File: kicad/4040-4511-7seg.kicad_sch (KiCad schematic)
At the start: 3 parts, among them U10 4511, U11 D168K, U12 4040

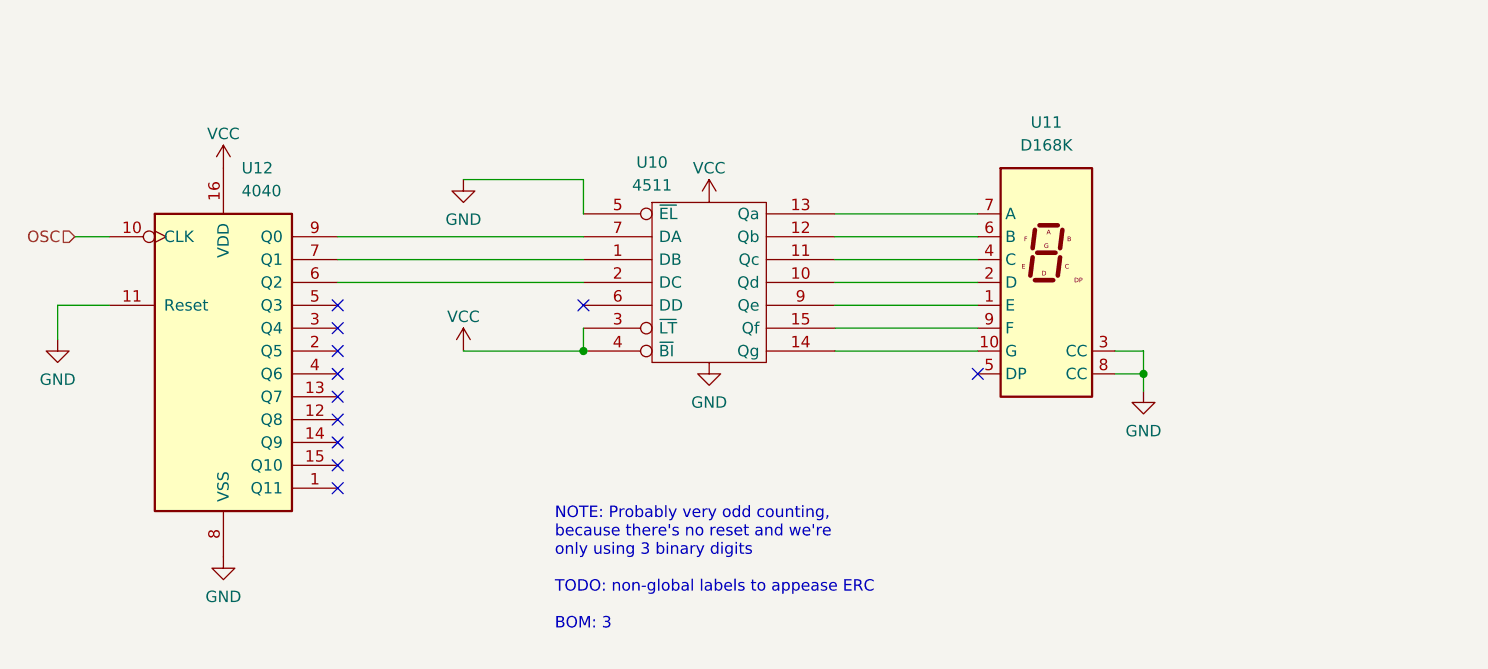
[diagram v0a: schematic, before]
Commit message: Hmmm, may need resistors for LED driver ICs
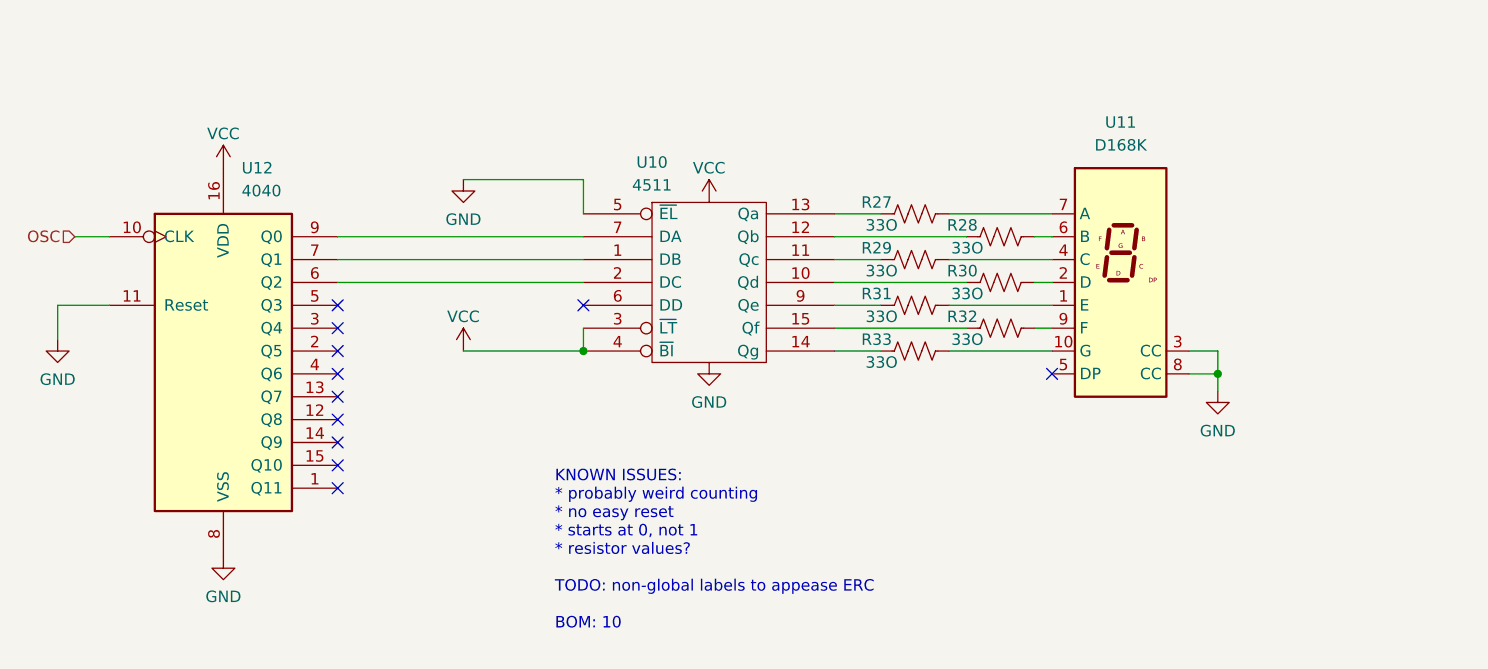
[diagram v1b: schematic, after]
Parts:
- added R27, R28, R29, R30, R31, R32, R33: 33O, Resistor_THT:R_Axial_DIN0204_L3.6mm_D1.6mm_P7.62mm_Horizontal, symbol Device:R_US
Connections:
- net at U10.10 (Qd): now also R30.1; no longer U11.2 (D)
- net at U10.11 (Qc): now also R29.1; no longer U11.4 (C)
- net at U10.12 (Qb): now also R28.1; no longer U11.6 (B)
- net at U10.13 (Qa): now also R27.1; no longer U11.7 (A)
- net at U10.14 (Qg): now also R33.1; no longer U11.10 (G)
- net at U10.15 (Qf): now also R32.1; no longer U11.9 (F)
- net at U10.9 (Qe): now also R31.1; no longer U11.1 (E)
- new net: R28.2, U11.6 (B)
- new net: R33.2, U11.10 (G)
- new net: R30.2, U11.2 (D)
- new net: R32.2, U11.9 (F)
- new net: R31.2, U11.1 (E)
- new net: R29.2, U11.4 (C)
- new net: R27.2, U11.7 (A)
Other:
- note added: "KNOWN ISSUES: * probably weird counting * no easy reset * starts at 0, not 1 * resistor values? TODO: non-global labels to appease ERC BOM: 10"
- note removed: "NOTE: Probably very odd counting, because there's no reset and we're only using 3 binary digits TODO: non-global labels to appease ERC BOM: 3"

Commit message: TODO: fix 7seg footprint
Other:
- note added: "TODO: fix footprint! 10 A 9 B 7 C 5 D 4 E 2 F 1 G 6 DP 3 COM 8 COM"
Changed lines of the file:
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@@
+    (effects (font (size 1.27 1.27)) (justify left bottom))
+  )
+  (text "TODO: fix footprint!\n\n10 A\n9  B\n7  C\n5  D\n4  E\n2  F\n1  G\n\n6  DP\n3  COM\n8  COM"
+    (at 215.265 83.82 0)
     (effects (font (size 1.27 1.27)) (justify left bottom))
   )

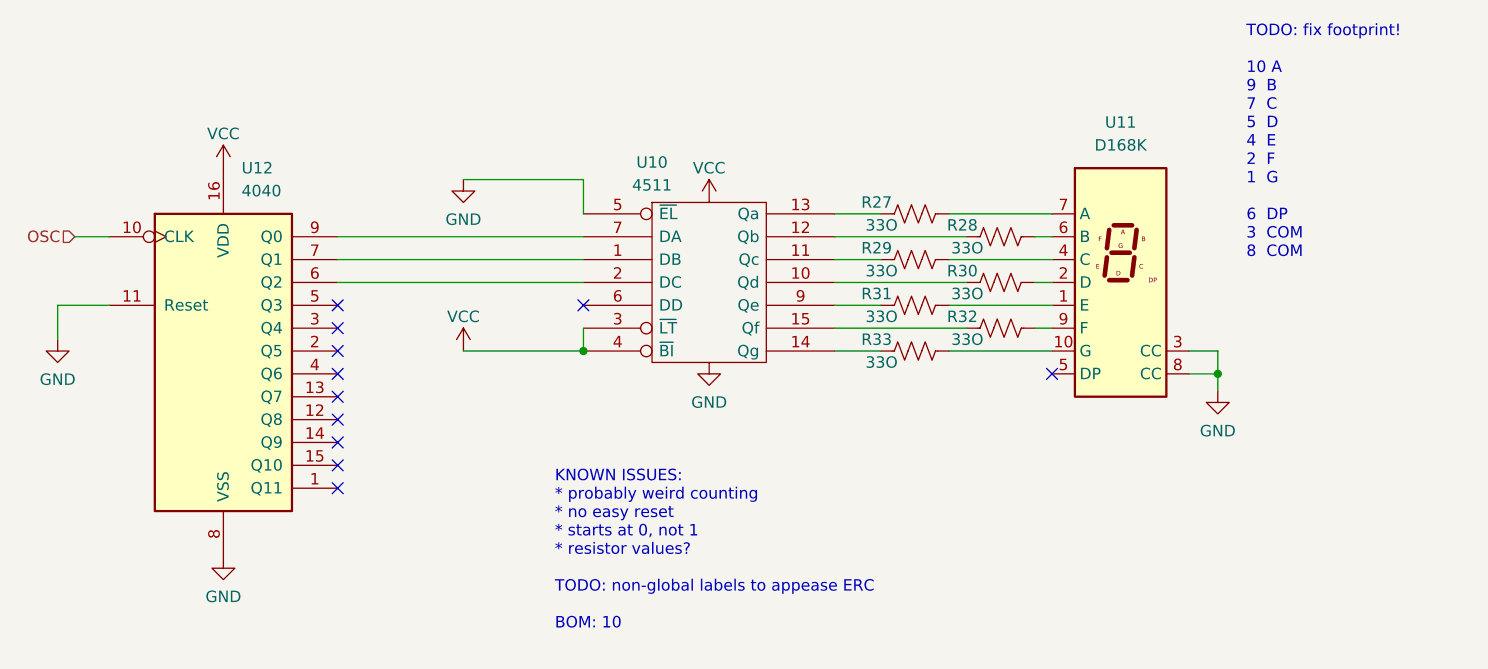
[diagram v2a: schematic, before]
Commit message: Fix 7seg footprint
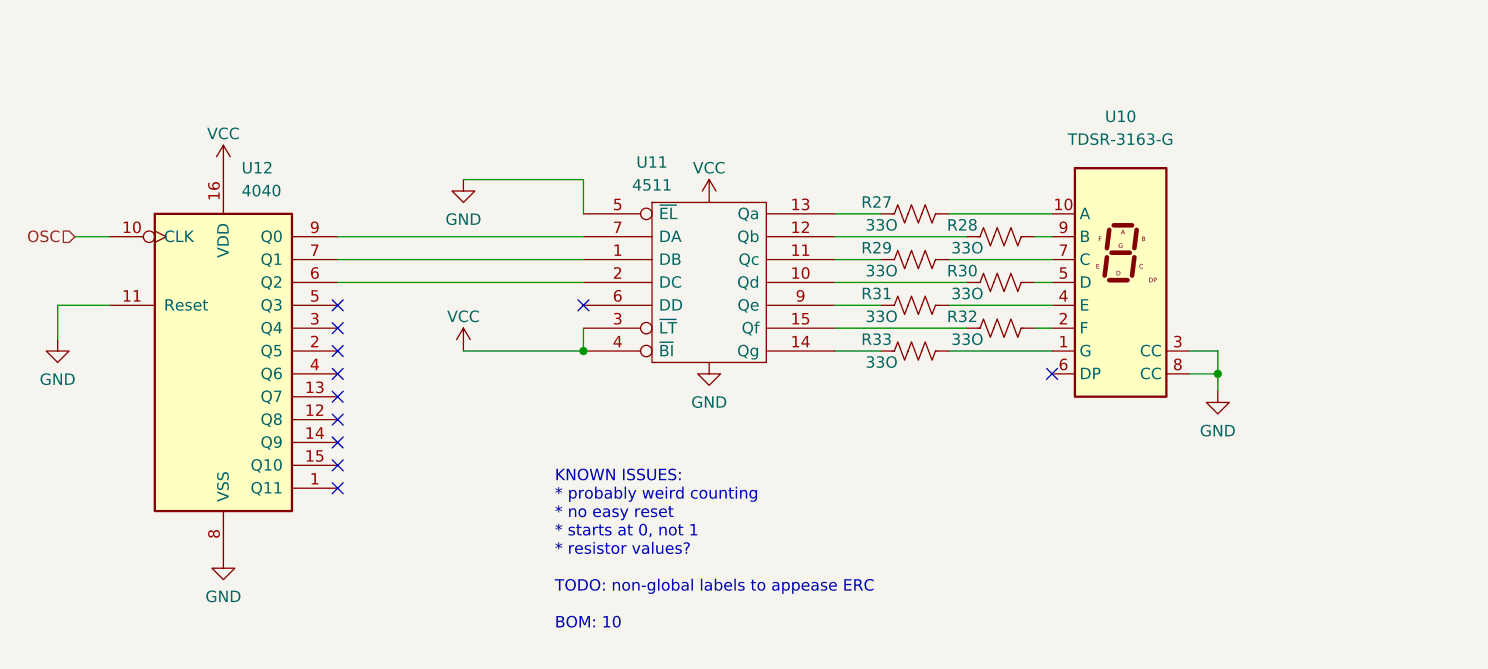
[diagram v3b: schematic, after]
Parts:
- removed U11: D168K, Display_7Segment:D1X8K, symbol Display_Character:D168K
- added U10: TDSR-3163-G, symbol parts_cafe:TDSR-3163-G
- renumbered U10 to U11
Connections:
- net GND: now also U10.3 (CC), U10.8 (CC)
- net at R28.2: now also U10.9 (B)
- net at R33.2: now also U10.1 (G)
- net at R30.2: now also U10.5 (D)
- net at R32.2: now also U10.2 (F)
- net at R31.2: now also U10.4 (E)
- net at R29.2: now also U10.7 (C)
- net at R27.2: now also U10.10 (A)
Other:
- note removed: "TODO: fix footprint! 10 A 9 B 7 C 5 D 4 E 2 F 1 G 6 DP 3 COM 8 COM"
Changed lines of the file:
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@@
-    (effects (font (size 1.27 1.27)) (justify left bottom))
-  )
-  (text "TODO: fix footprint!\n\n10 A\n9  B\n7  C\n5  D\n4  E\n2  F\n1  G\n\n6  DP\n3  COM\n8  COM"
-    (at 215.265 83.82 0)
     (effects (font (size 1.27 1.27)) (justify left bottom))
   )
@@
     (pin "1")
   )
+  (symbol (lib_id "parts_cafe:TDSR-3163-G") (at 196.215 72.39 0) (unit 1)
+    (in_bom yes) (on_board yes) (fields_autoplaced)
+    (property "Reference" "U10" (id 0) (at 201.295 67.945 0))
+    (property "Value" "TDSR-3163-G" (id 1) (at 201.295 70.485 0))
+    (property "Footprint" "" (id 2) (at 196.215 72.39 0)
+      (effects (font (size 1.27 1.27)) hide)
+    )
+    (property "Datasheet" "" (id 3) (at 196.215 72.39 0)
+      (effects (font (size 1.27 1.27)) hide)
+    )
+    (pin "1")
+    (pin "10")
+    (pin "2")
+    (pin "3")
+    (pin "4")
+    (pin "5")
+    (pin "6")
+    (pin "7")
+    (pin "8")
+    (pin "9")
+  )
   (symbol (lib_id "Device:R_US") (at 178.435 83.82 90) (unit 1)
     (in_bom yes) (on_board yes)
@@
   (symbol (lib_id "4xxx_IEEE:4511") (at 155.575 86.36 0) (unit 1)
     (in_bom yes) (on_board yes)
-    (property "Reference" "U10" (id 0) (at 149.225 73.025 0))
+    (property "Reference" "U11" (id 0) (at 149.225 73.025 0))
     (property "Value" "4511" (id 1) (at 149.225 75.565 0))
     (property "Footprint" "" (id 2) (at 155.575 86.36 0)
@@
     (pin "2")
     (pin "3")
-    (pin "4")
-    (pin "5")
-    (pin "6")
-    (pin "7")
-    (pin "8")
-    (pin "9")
-  )
-  (symbol (lib_id "Display_Character:D168K") (at 201.295 86.36 0) (unit 1)
-    (in_bom yes) (on_board yes) (fields_autoplaced)
-    (property "Reference" "U11" (id 0) (at 201.295 68.58 0))
-    (property "Value" "D168K" (id 1) (at 201.295 71.12 0))
-    (property "Footprint" "Display_7Segment:D1X8K" (id 2) (at 201.295 101.6 0)
-      (effects (font (size 1.27 1.27)) hide)
-    )
-    (property "Datasheet" "https://ia800903.us.archive.org/24/items/CTKD1x8K/Cromatek%20D168K.pdf" (id 3) (at 188.595 74.295 0)
-      (effects (font (size 1.27 1.27)) (justify left) hide)
-    )
-    (pin "1")
-    (pin "10")
-    (pin "2")
-    (pin "3")

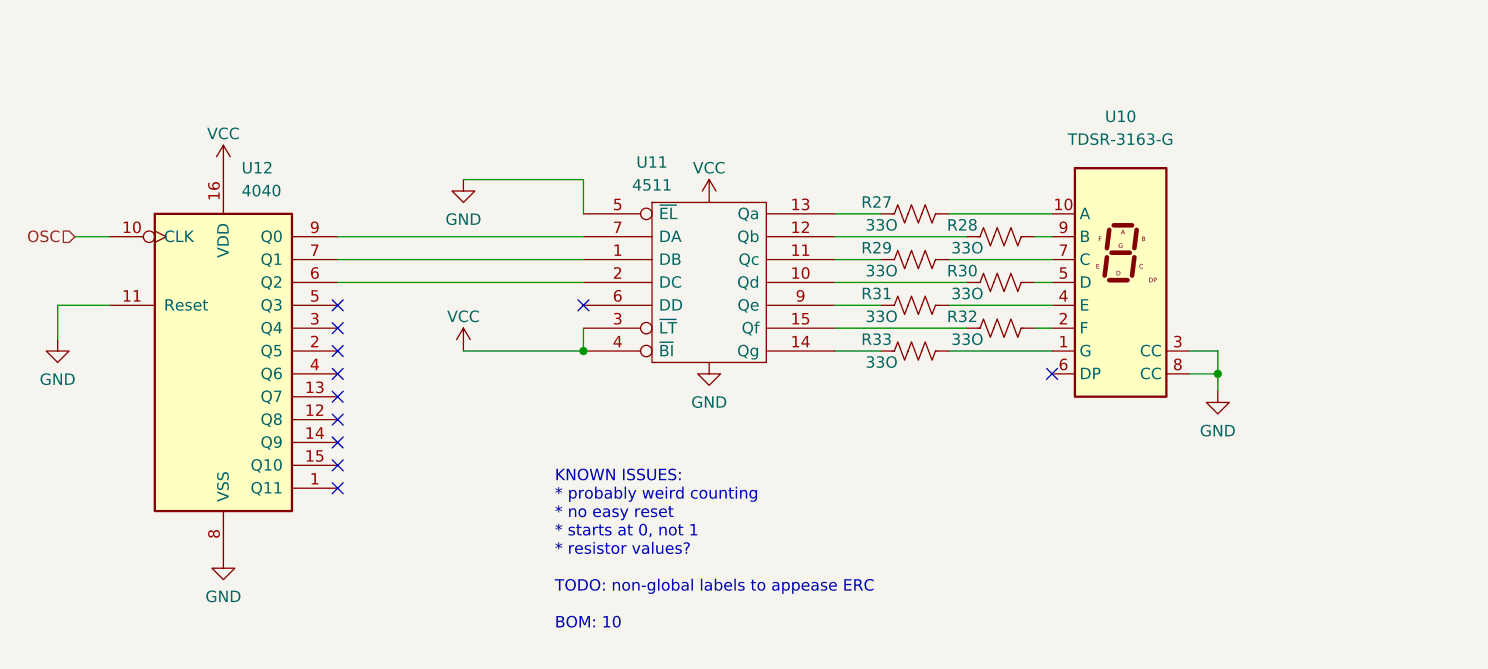
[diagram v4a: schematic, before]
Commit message: Update to latest kicad
no functional changes
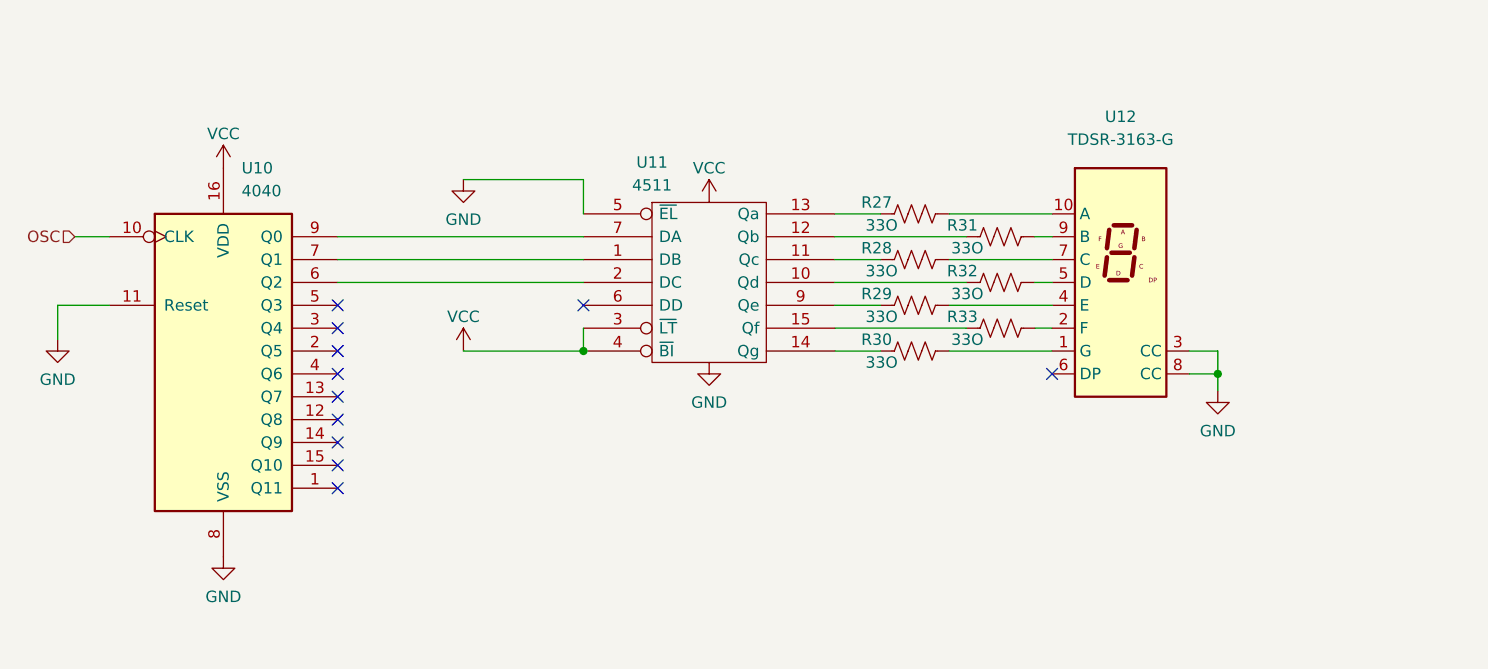
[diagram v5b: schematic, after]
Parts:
- renumbered R29 to R28, R31 to R29, R33 to R30, R28 to R31, R30 to R32, R32 to R33, U12 to U10, U10 to U12
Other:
- note removed: "KNOWN ISSUES: * probably weird counting * no easy reset * starts at 0, not 1 * resistor values? TODO: non-global labels to appease ERC BOM: 10"

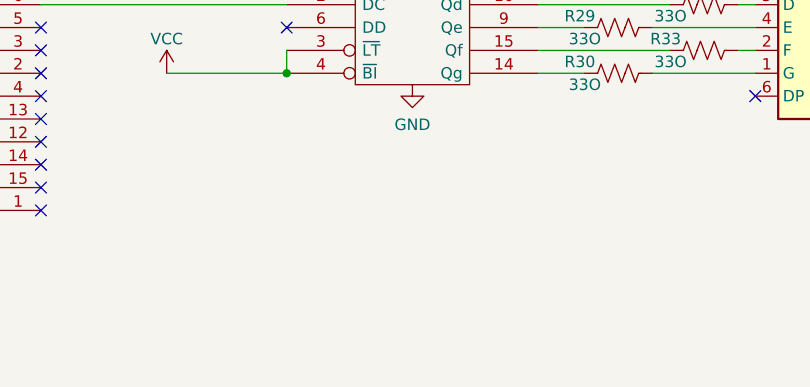
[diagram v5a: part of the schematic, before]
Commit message: Add CD4029 to CD4511 to 7seg schematic
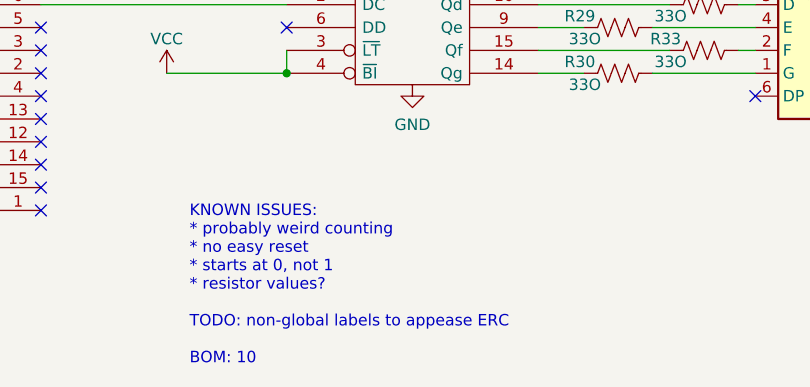
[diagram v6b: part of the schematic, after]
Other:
- note added: "KNOWN ISSUES: * probably weird counting * no easy reset * starts at 0, not 1 * resistor values? TODO: non-global labels to appease ERC BOM: 10"
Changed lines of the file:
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@@
 	(generator_version "9.0")
 	(paper "A4")
+	(text "KNOWN ISSUES:\n* probably weird counting\n* no easy reset\n* starts at 0, not 1\n* resistor values?\n\nTODO: non-global labels to appease ERC\n\nBOM: 10"
+		(exclude_from_sim no)
+		(at 130.81 126.492 0)
+		(effects
+			(font
+				(size 1.27 1.27)
+			)
+			(justify left bottom)
+		)
+	)
 	(junction
 		(at 212.09 96.52)
